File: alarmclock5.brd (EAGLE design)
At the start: 60 x 92 mm, 48 parts, among them Q1 FDN360P, T1 2N2222, X1 MKDSN1,5/2-5,08, X2 MKDSN1,5/2-5,08, X3 MKDSN1,5/2-5,08, X4 MKDSN1,5/2-5,08

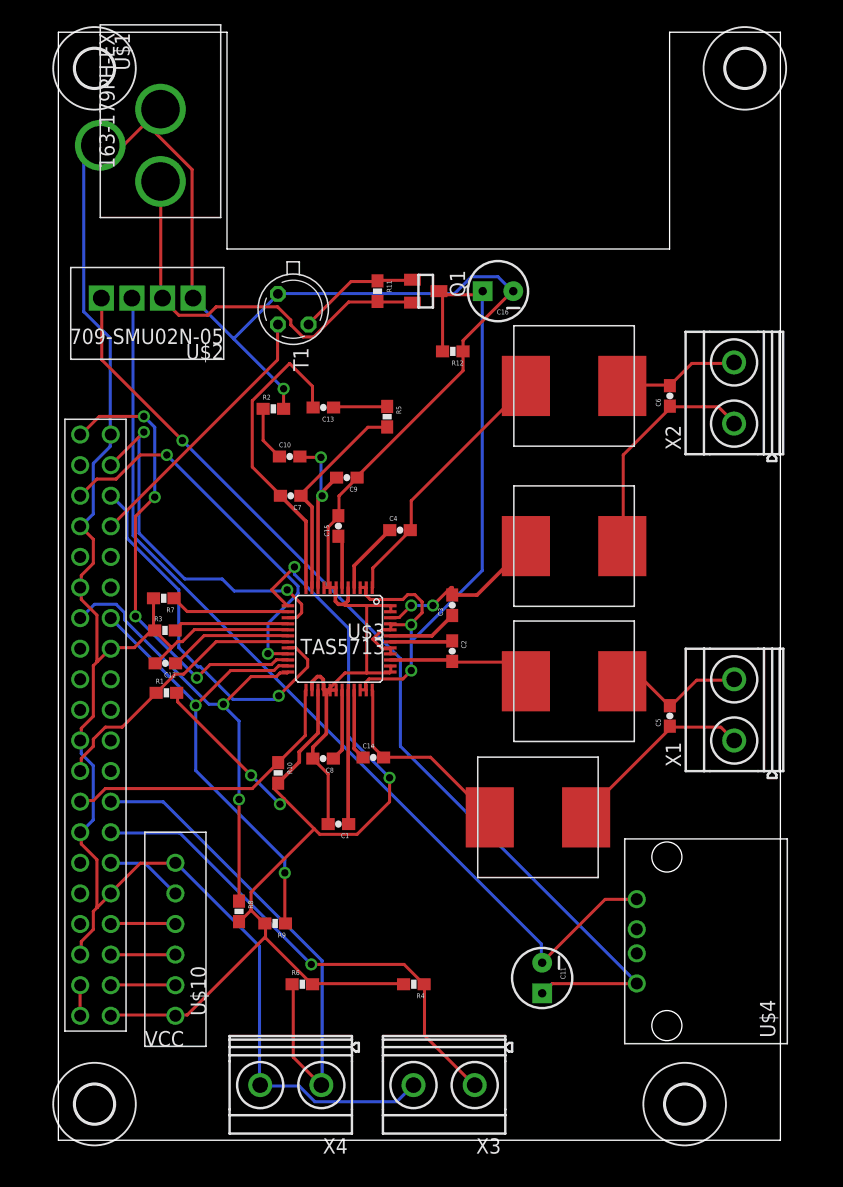
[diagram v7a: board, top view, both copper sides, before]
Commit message: new decoupling capa
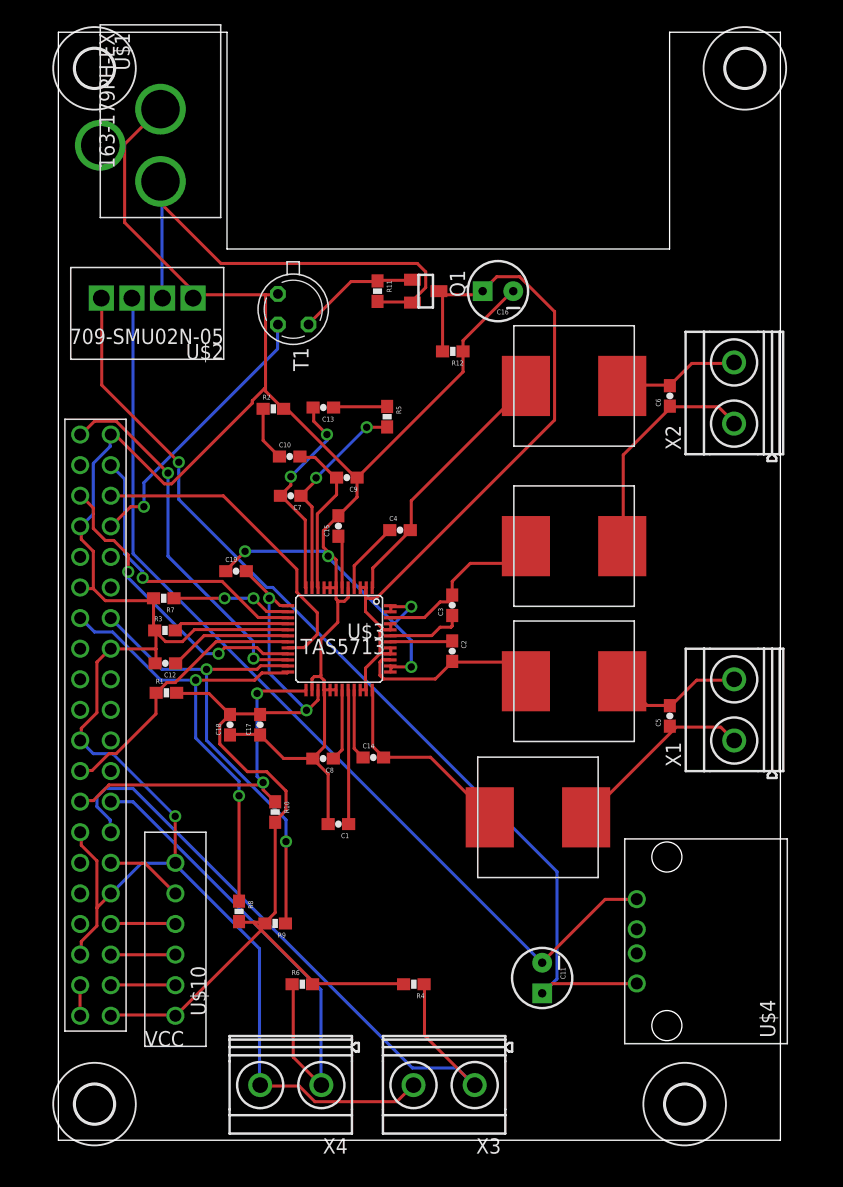
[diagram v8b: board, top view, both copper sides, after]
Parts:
- added C17, C19: 10uF25V, SparkFun-Capacitors:0603-CAP
- added C18: 0.1uF25V, SparkFun-Capacitors:0603-CAP
- C1: value 0.1uF25V -> 1uF25V
- moved R10 3.26 mm to (18.0, 27.2)
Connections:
- net +3V3: now also C17.2, C18.2, C19.2
- net GND: now also C17.1, C18.1, C19.1
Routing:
- net +3V3: track 104.6 -> 83.6 mm, vias 4 -> 2
- net N$8: track 41.4 -> 55.4 mm, vias 1 -> 0
- net GND: track 270.3 -> 281.7 mm, vias 1 -> 5
- net N$22: track 26.2 -> 18.0 mm, vias 0 -> 2
- net N$1: track 38.9 -> 30.8 mm, vias 4 -> 2
- net N$43: track 34.2 -> 41.9 mm
- net N$5: track 32.3 -> 25.2 mm
- net N$2: track 30.5 -> 23.9 mm, vias 2 -> 1
- net N$37: track 24.8 -> 29.7 mm, vias 0 -> 2
- net N$4: track 31.2 -> 27.0 mm, vias 1 -> 0
- net VCC: track 64.8 -> 60.8 mm, vias 2 -> 0
- net N$16: track 12.0 -> 15.6 mm
- net N$6: track 42.8 -> 41.3 mm
- net N$23: track 15.0 -> 13.6 mm, vias 2 -> 0
- net N$3: track 83.5 -> 82.4 mm
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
